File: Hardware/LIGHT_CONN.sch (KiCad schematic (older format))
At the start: 49 parts, among them P10 -15V, P11 ~4, P12 1, P13 ~5, P14 +5V, P18 RX7, P19 3.3V, P20 TX6, P21 1.8V, P22 PSU_CTL, P23 GND, P27 D1, P29 D2, P30 D3, P31 P1, P32 L1.8_1, P33 L3.3_1, P34 P2, P35 L1.8_2, P36 L3.3_2, P37 P3, P38 L1.8_3, P39 L3.3_3, P40 P4, P41 L1.8_4, P42 L3.3_4, P6 CONN_02X14, P7 ~2, P8 +15V, P9 ~3, U22 PCA9685BS

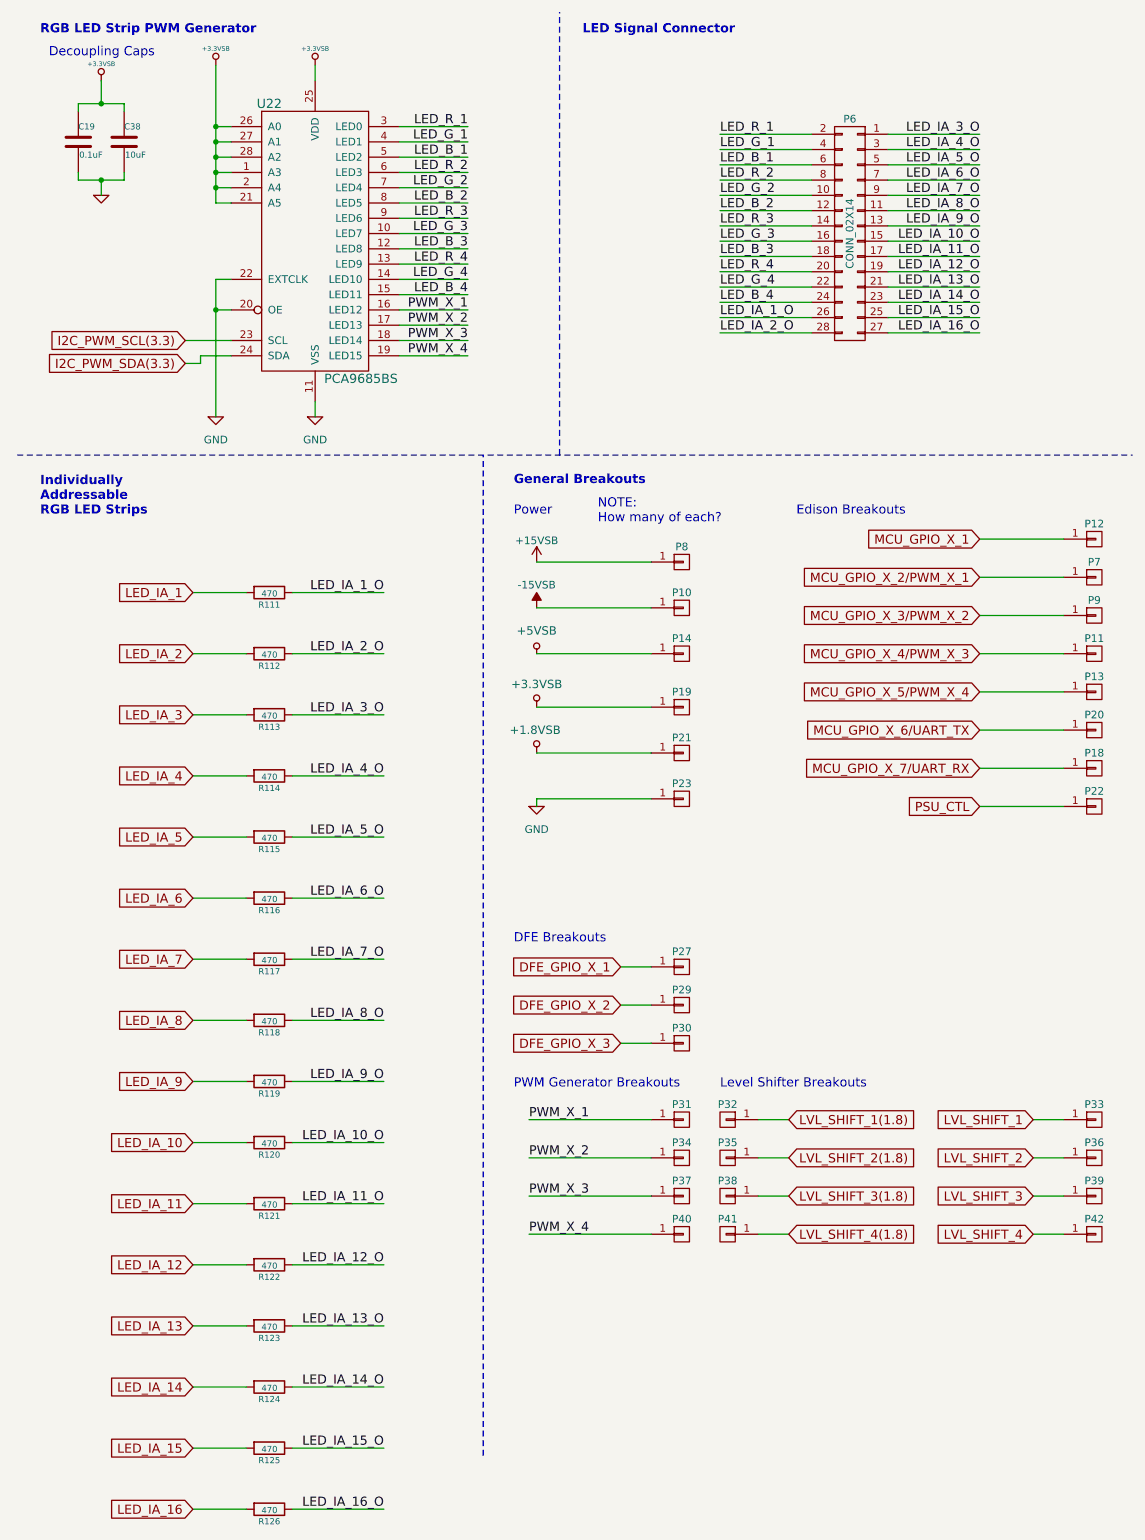
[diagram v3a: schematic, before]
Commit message: Digital Half completed placement
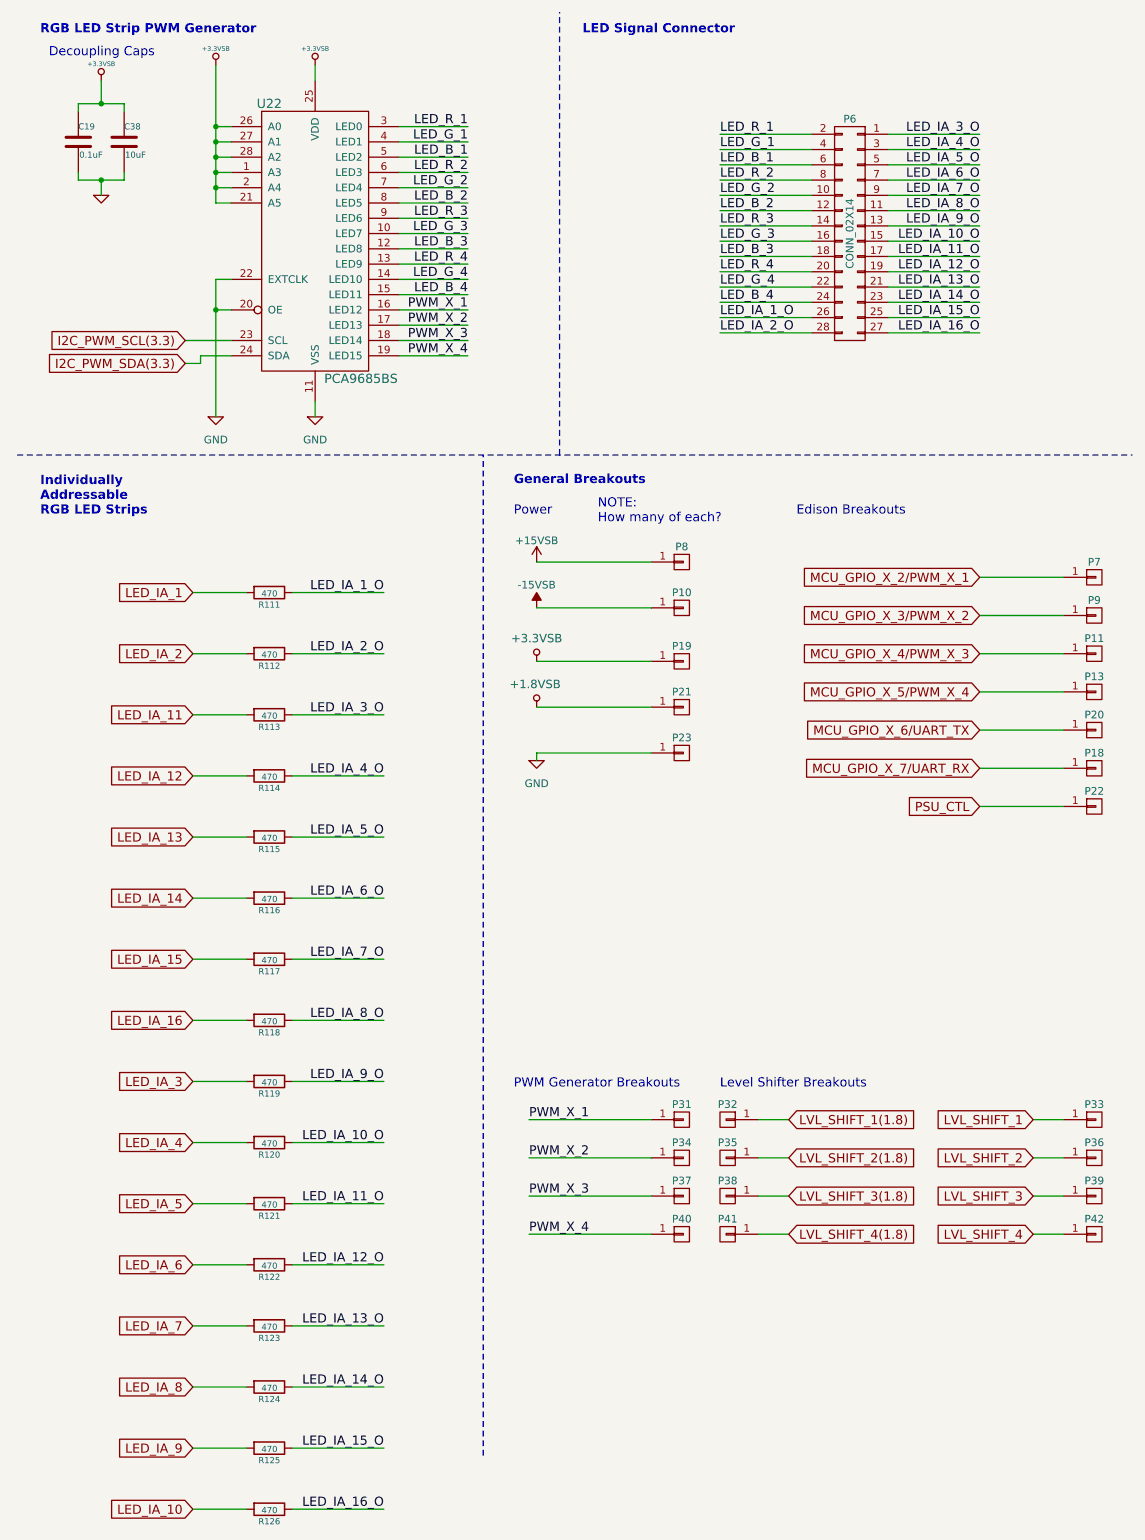
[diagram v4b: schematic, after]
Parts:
- removed P12: 1, Pin_Headers:Pin_Header_Straight_1x01, symbol CONN_01X01
- removed P14: +5V, Pin_Headers:Pin_Header_Straight_1x01, symbol CONN_01X01
- removed P27: D1, Pin_Headers:Pin_Header_Straight_1x01, symbol CONN_01X01
- removed P29: D2, Pin_Headers:Pin_Header_Straight_1x01, symbol CONN_01X01
- removed P30: D3, Pin_Headers:Pin_Header_Straight_1x01, symbol CONN_01X01
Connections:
- net LED_IA_10: now also R126.2; no longer R120.2
- net LED_IA_11: now also R113.2; no longer R121.2
- net LED_IA_12: now also R114.2; no longer R122.2
- net LED_IA_13: now also R115.2; no longer R123.2
- net LED_IA_14: now also R116.2; no longer R124.2
- net LED_IA_15: now also R117.2; no longer R125.2
- net LED_IA_16: now also R118.2; no longer R126.2
- net LED_IA_3: now also R119.2; no longer R113.2
- net LED_IA_4: now also R120.2; no longer R114.2
- net LED_IA_5: now also R121.2; no longer R115.2
- net LED_IA_6: now also R122.2; no longer R116.2
- net LED_IA_7: now also R123.2; no longer R117.2
- net LED_IA_8: now also R124.2; no longer R118.2
- net LED_IA_9: now also R125.2; no longer R119.2
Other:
- note removed: "DFE Breakouts"
- moved on the sheet: P19, P21, P23
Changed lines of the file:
@@
 $EndComp
 $Comp
-L GND-RESCUE-museV2-RESCUE-museV2 #PWR0118
+L GND-RESCUE-museV2-RESCUE-museV2 #PWR0114
 U 1 1 57E62373
 P 2450 3150
-F 0 "#PWR0118" H 2450 2900 50  0001 C CNN
+F 0 "#PWR0114" H 2450 2900 50  0001 C CNN
 F 1 "GND" H 2450 3000 50  0000 C CNN
 F 2 "" H 2450 3150 50  0000 C CNN
@@
 	1650 4700 2000 4700
 Wire Wire Line
+	1650 7500 2000 7500
+Wire Wire Line
+	1650 7900 2000 7900
+Wire Wire Line
+	1650 8300 2000 8300
+Wire Wire Line
+	1650 8700 2000 8700
+Wire Wire Line
+	1650 9100 2000 9100
+Wire Wire Line
+	1650 9500 2000 9500
+Wire Wire Line
+	1650 9900 2000 9900
+Wire Wire Line
+	1650 10300 2000 10300
+Wire Wire Line
 	1650 5100 2000 5100
 Wire Wire Line
@@
 Wire Wire Line
 	1650 7100 2000 7100
-Wire Wire Line
-	1650 7500 2000 7500
-Wire Wire Line
-	1650 7900 2000 7900
-Wire Wire Line
-	1650 8300 2000 8300
-Wire Wire Line
-	1650 8700 2000 8700
-Wire Wire Line
-	1650 9100 2000 9100
-Wire Wire Line
-	1650 9500 2000 9500
-Wire Wire Line
-	1650 9900 2000 9900
-Wire Wire Line
-	1650 10300 2000 10300
 Text Notes 650  650  0    60   ~ 12
 RGB LED Strip PWM Generator
@@
 Connection ~ 1800 1250
 $Comp
-L GND-RESCUE-museV2-RESCUE-museV2 #PWR0119
+L GND-RESCUE-museV2-RESCUE-museV2 #PWR0115
 U 1 1 57EF1660
 P 1800 3150
-F 0 "#PWR0119" H 1800 2900 50  0001 C CNN
+F 0 "#PWR0115" H 1800 2900 50  0001 C CNN
 F 1 "GND" H 1800 3000 50  0000 C CNN
 F 2 "" H 1800 3150 50  0000 C CNN
@@
 Text GLabel 1650 4700 0    60   Input ~ 0
 LED_IA_2
+Text GLabel 1650 7500 0    60   Input ~ 0
+LED_IA_3
+Text GLabel 1650 7900 0    60   Input ~ 0
+LED_IA_4
+Text GLabel 1650 8300 0    60   Input ~ 0
+LED_IA_5
+Text GLabel 1650 8700 0    60   Input ~ 0
+LED_IA_6
+Text GLabel 1650 9100 0    60   Input ~ 0
+LED_IA_7
+Text GLabel 1650 9500 0    60   Input ~ 0
+LED_IA_8
+Text GLabel 1650 9900 0    60   Input ~ 0
+LED_IA_9
+Text GLabel 1650 10300 0    60   Input ~ 0
+LED_IA_10
 Text GLabel 1650 5100 0    60   Input ~ 0
-LED_IA_3
+LED_IA_11
 Text GLabel 1650 5500 0    60   Input ~ 0
-LED_IA_4
+LED_IA_12
 Text GLabel 1650 5900 0    60   Input ~ 0
-LED_IA_5
+LED_IA_13
 Text GLabel 1650 6300 0    60   Input ~ 0
-LED_IA_6
+LED_IA_14
 Text GLabel 1650 6700 0    60   Input ~ 0
-LED_IA_7
+LED_IA_15
 Text GLabel 1650 7100 0    60   Input ~ 0
-LED_IA_8
-Text GLabel 1650 7500 0    60   Input ~ 0
-LED_IA_9
-Text GLabel 1650 7900 0    60   Input ~ 0
-LED_IA_10
-Text GLabel 1650 8300 0    60   Input ~ 0
-LED_IA_11
-Text GLabel 1650 8700 0    60   Input ~ 0
-LED_IA_12
-Text GLabel 1650 9100 0    60   Input ~ 0
-LED_IA_13
-Text GLabel 1650 9500 0    60   Input ~ 0
-LED_IA_14
-Text GLabel 1650 9900 0    60   Input ~ 0
-LED_IA_15
-Text GLabel 1650 10300 0    60   Input ~ 0
 LED_IA_16
 Wire Wire Line
@@
 $EndComp
 $Comp
-L +15VSB #PWR0120
+L +15VSB #PWR0116
 U 1 1 57FFBADE
 P 3900 4100
-F 0 "#PWR0120" H 3900 3950 50  0001 C CNN
+F 0 "#PWR0116" H 3900 3950 50  0001 C CNN
 F 1 "+15VSB" H 3900 4240 50  0000 C CNN
 F 2 "" H 3900 4100 50  0000 C CNN
@@
 	4650 4400 3900 4400
 $Comp
-L -15VSB #PWR134
+L -15VSB #PWR130
 U 1 1 57FFBC18
 P 3900 4400
-F 0 "#PWR134" H 3900 4500 50  0001 C CNN
+F 0 "#PWR130" H 3900 4500 50  0001 C CNN
 F 1 "-15VSB" H 3900 4550 50  0000 C CNN
 F 2 "" H 3900 4400 50  0000 C CNN
@@
 $EndComp
 $Comp
-L CONN_01X01 P14
-U 1 1 57FFBEAF
-P 4850 4700
-F 0 "P14" H 4850 4800 50  0000 C CNN
-F 1 "+5V" V 4950 4700 50  0001 C CNN
-F 2 "Pin_Headers:Pin_Header_Straight_1x01" H 4850 4700 50  0001 C CNN
-F 3 "" H 4850 4700 50  0000 C CNN
-	1    4850 4700
-	1    0    0    -1
-$EndComp
-Wire Wire Line
-	4650 4700 3900 4700
-$Comp
-L +5VSB #PWR0121
-U 1 1 57FFD044
-P 3900 4700
-F 0 "#PWR0121" H 3900 4790 20  0001 C CNN
-F 1 "+5VSB" H 3900 4850 55  0000 C CNN
-F 2 "" H 3900 4700 60  0000 C CNN
-F 3 "" H 3900 4700 60  0000 C CNN
-	1    3900 4700
-	1    0    0    -1
-$EndComp
-$Comp
 L CONN_01X01 P19
 U 1 1 57FFE1F7
+P 4850 4750
+F 0 "P19" H 4850 4850 50  0000 C CNN
+F 1 "3.3V" V 4950 4750 50  0001 C CNN
+F 2 "Pin_Headers:Pin_Header_Straight_1x01" H 4850 4750 50  0001 C CNN
+F 3 "" H 4850 4750 50  0000 C CNN
+	1    4850 4750
+	1    0    0    -1
+$EndComp
+Wire Wire Line
+	4650 4750 3900 4750
+$Comp
+L +3.3VSB #PWR0117
+U 1 1 57FFEA10
+P 3900 4750
+F 0 "#PWR0117" H 3900 4710 30  0001 C CNN
+F 1 "+3.3VSB" H 3900 4900 55  0000 C CNN
+F 2 "" H 3900 4750 60  0000 C CNN
+F 3 "" H 3900 4750 60  0000 C CNN
+	1    3900 4750
+	1    0    0    -1
+$EndComp
+$Comp
+L CONN_01X01 P21
+U 1 1 57FFEA97
 P 4850 5050
-F 0 "P19" H 4850 5150 50  0000 C CNN
-F 1 "3.3V" V 4950 5050 50  0001 C CNN
+F 0 "P21" H 4850 5150 50  0000 C CNN
+F 1 "1.8V" V 4950 5050 50  0001 C CNN
 F 2 "Pin_Headers:Pin_Header_Straight_1x01" H 4850 5050 50  0001 C CNN
 F 3 "" H 4850 5050 50  0000 C CNN
@@
 	4650 5050 3900 5050
 $Comp
-L +3.3VSB #PWR0122
-U 1 1 57FFEA10
+L +1.8VSB #PWR0118
+U 1 1 57FFEE42
 P 3900 5050
-F 0 "#PWR0122" H 3900 5010 30  0001 C CNN
-F 1 "+3.3VSB" H 3900 5200 55  0000 C CNN
+F 0 "#PWR0118" H 3900 5190 20  0001 C CNN
+F 1 "+1.8VSB" H 3890 5200 55  0000 C CNN
 F 2 "" H 3900 5050 60  0000 C CNN
 F 3 "" H 3900 5050 60  0000 C CNN
@@
 $EndComp
 $Comp
-L CONN_01X01 P21
-U 1 1 57FFEA97
+L CONN_01X01 P23
+U 1 1 57FFF0C1
 P 4850 5350
-F 0 "P21" H 4850 5450 50  0000 C CNN
-F 1 "1.8V" V 4950 5350 50  0001 C CNN
+F 0 "P23" H 4850 5450 50  0000 C CNN
+F 1 "GND" V 4950 5350 50  0001 C CNN
 F 2 "Pin_Headers:Pin_Header_Straight_1x01" H 4850 5350 50  0001 C CNN
 F 3 "" H 4850 5350 50  0000 C CNN
@@
 	4650 5350 3900 5350
 $Comp
-L +1.8VSB #PWR0123
-U 1 1 57FFEE42
-P 3900 5350
-F 0 "#PWR0123" H 3900 5490 20  0001 C CNN
-F 1 "+1.8VSB" H 3890 5500 55  0000 C CNN
-F 2 "" H 3900 5350 60  0000 C CNN
-F 3 "" H 3900 5350 60  0000 C CNN
-	1    3900 5350
-	1    0    0    -1
-$EndComp
-$Comp
-L CONN_01X01 P23
-U 1 1 57FFF0C1
-P 4850 5650
-F 0 "P23" H 4850 5750 50  0000 C CNN
-F 1 "GND" V 4950 5650 50  0001 C CNN
-F 2 "Pin_Headers:Pin_Header_Straight_1x01" H 4850 5650 50  0001 C CNN
-F 3 "" H 4850 5650 50  0000 C CNN
-	1    4850 5650
-	1    0    0    -1
-$EndComp
-Wire Wire Line
-	4650 5650 3900 5650
-$Comp
-L GND-RESCUE-museV2-RESCUE-museV2 #PWR0124
+L GND-RESCUE-museV2-RESCUE-museV2 #PWR0119
 U 1 1 57FFF105
-P 3900 5700
-F 0 "#PWR0124" H 3900 5450 50  0001 C CNN
-F 1 "GND" H 3900 5550 50  0000 C CNN
-F 2 "" H 3900 5700 50  0000 C CNN
-F 3 "" H 3900 5700 50  0000 C CNN
-	1    3900 5700
-	1    0    0    -1
-$EndComp
-Wire Wire Line
-	3900 5650 3900 5700
+P 3900 5400
+F 0 "#PWR0119" H 3900 5150 50  0001 C CNN
+F 1 "GND" H 3900 5250 50  0000 C CNN
+F 2 "" H 3900 5400 50  0000 C CNN
+F 3 "" H 3900 5400 50  0000 C CNN
+	1    3900 5400
+	1    0    0    -1
+$EndComp
+Wire Wire Line
+	3900 5350 3900 5400
 Text Notes 4300 3850 0    60   ~ 0
 NOTE:\nHow many of each?
 Text Notes 3750 3800 0    60   ~ 0
 Power
-Text GLabel 4450 6750 0    60   Input ~ 0
-DFE_GPIO_X_1
-Text GLabel 4450 7000 0    60   Input ~ 0
-DFE_GPIO_X_2
-Text GLabel 4450 7250 0    60   Input ~ 0
-DFE_GPIO_X_3
-$Comp
-L CONN_01X01 P30
-U 1 1 58004BCB
-P 4850 7250
-F 0 "P30" H 4850 7350 50  0000 C CNN
-F 1 "D3" V 4950 7250 50  0001 C CNN
-F 2 "Pin_Headers:Pin_Header_Straight_1x01" H 4850 7250 50  0001 C CNN
-F 3 "" H 4850 7250 50  0000 C CNN
-	1    4850 7250
-	1    0    0    -1
-$EndComp
-$Comp
-L CONN_01X01 P29
-U 1 1 58004C4E
-P 4850 7000
-F 0 "P29" H 4850 7100 50  0000 C CNN
-F 1 "D2" V 4950 7000 50  0001 C CNN
-F 2 "Pin_Headers:Pin_Header_Straight_1x01" H 4850 7000 50  0001 C CNN
-F 3 "" H 4850 7000 50  0000 C CNN
-	1    4850 7000
-	1    0    0    -1
-$EndComp
-$Comp
-L CONN_01X01 P27
-U 1 1 58004CB6
-P 4850 6750
-F 0 "P27" H 4850 6850 50  0000 C CNN
-F 1 "D1" V 4950 6750 50  0001 C CNN
-F 2 "Pin_Headers:Pin_Header_Straight_1x01" H 4850 6750 50  0001 C CNN
-F 3 "" H 4850 6750 50  0000 C CNN
-	1    4850 6750
-	1    0    0    -1
-$EndComp
-Wire Wire Line
-	4650 7000 4450 7000
-Wire Wire Line
-	4450 7250 4650 7250
-Text Notes 3750 6600 0    60   ~ 0
-DFE Breakouts
 Text Notes 5600 3800 0    60   ~ 0
 Edison Breakouts
@@
 Text GLabel 6800 5200 0    60   Input ~ 0
 MCU_GPIO_X_6/UART_TX
-Wire Wire Line
-	4450 6750 4650 6750
 Text Notes 5100 7550 0    60   ~ 0
 Level Shifter Breakouts
@@
 Text GLabel 6800 5700 0    60   Input ~ 0
 PSU_CTL
-Text GLabel 6800 3950 0    60   Input ~ 0
-MCU_GPIO_X_1
-$Comp
-L CONN_01X01 P12
-U 1 1 5862A3DE
-P 7550 3950
-F 0 "P12" H 7550 4050 50  0000 C CNN
-F 1 "1" V 7650 3950 50  0001 C CNN
-F 2 "Pin_Headers:Pin_Header_Straight_1x01" H 7550 3950 50  0001 C CNN
-F 3 "" H 7550 3950 50  0000 C CNN
-	1    7550 3950
-	1    0    0    -1
-$EndComp
-Wire Wire Line
-	7350 3950 6800 3950
-$Comp
-L +3.3VSB #PWR0125
+$Comp
+L +3.3VSB #PWR0120
 U 1 1 5862B130
 P 1800 850
-F 0 "#PWR0125" H 1800 810 30  0001 C CNN
+F 0 "#PWR0120" H 1800 810 30  0001 C CNN
 F 1 "+3.3VSB" H 1800 960 30  0000 C CNN
 F 2 "" H 1800 850 60  0000 C CNN
@@
 $EndComp
 $Comp
-L +3.3VSB #PWR0126
+L +3.3VSB #PWR0121
 U 1 1 5862B1CF
 P 2450 850
-F 0 "#PWR0126" H 2450 810 30  0001 C CNN
+F 0 "#PWR0121" H 2450 810 30  0001 C CNN
 F 1 "+3.3VSB" H 2450 960 30  0000 C CNN
 F 2 "" H 2450 850 60  0000 C CNN
@@
 $EndComp
 $Comp
-L +3.3VSB #PWR0127
+L +3.3VSB #PWR0122
 U 1 1 5862D3DB
 P 1050 950
-F 0 "#PWR0127" H 1050 910 30  0001 C CNN
+F 0 "#PWR0122" H 1050 910 30  0001 C CNN
 F 1 "+3.3VSB" H 1050 1060 30  0000 C CNN
 F 2 "" H 1050 950 60  0000 C CNN
@@
 	1200 1600 1200 1550
 $Comp
-L GND #PWR0128
+L GND #PWR0123
 U 1 1 5862D6A9
 P 1050 1700
-F 0 "#PWR0128" H 1050 1700 30  0001 C CNN
+F 0 "#PWR0123" H 1050 1700 30  0001 C CNN
 F 1 "GND" H 1050 1630 30  0001 C CNN
 F 2 "" H 1050 1700 60  0000 C CNN

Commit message: Beginning analog chip placement
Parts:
- C38: footprint Capacitors_SMD:C_1206 -> Capacitors_SMD:c_elec_4x5.3
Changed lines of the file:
@@
 F 0 "C38" H 1200 1450 40  0000 L CNN
 F 1 "10uF" H 1206 1265 40  0000 L CNN
-F 2 "Capacitors_SMD:C_1206" H 1238 1200 30  0001 C CNN
+F 2 "Capacitors_SMD:c_elec_4x5.3" H 1238 1200 30  0001 C CNN
 F 3 "" H 1200 1350 60  0000 C CNN
 	1    1200 1350

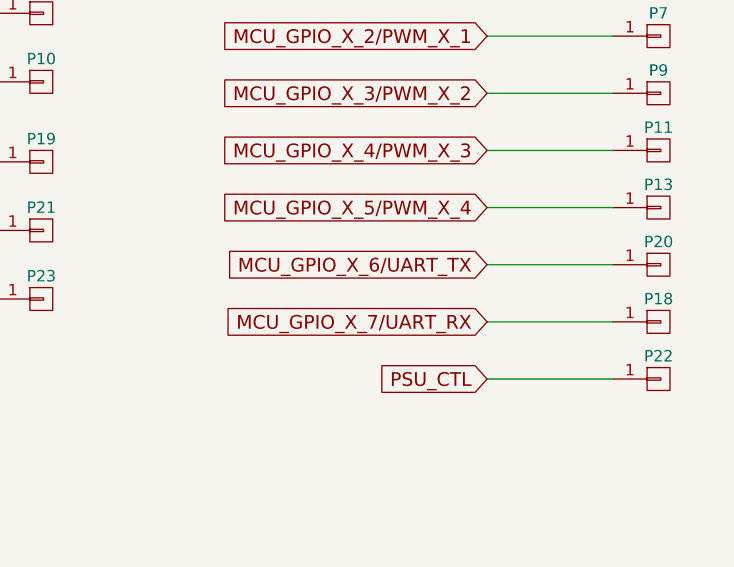
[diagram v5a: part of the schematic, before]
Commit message: All tracks and planes filled.  Fixing fill intersections and missing power/gnd connections
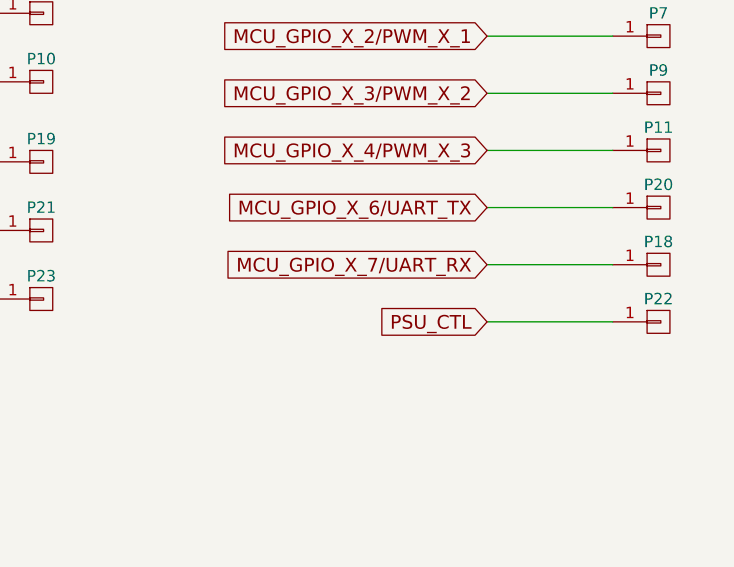
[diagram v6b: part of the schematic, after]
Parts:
- removed P13: ~5, Pin_Headers:Pin_Header_Straight_1x01, symbol CONN_01X01
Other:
- moved on the sheet: P18, P20, P22
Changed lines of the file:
@@
 Wire Wire Line
 	6800 4700 7350 4700
-$Comp
-L CONN_01X01 P13
-U 1 1 58007233
+Text GLabel 6800 5200 0    60   Input ~ 0
+MCU_GPIO_X_7/UART_RX
+$Comp
+L CONN_01X01 P20
+U 1 1 58007A71
 P 7550 4950
-F 0 "P13" H 7550 5050 50  0000 C CNN
-F 1 "~5" V 7650 4950 50  0001 C CNN
+F 0 "P20" H 7550 5050 50  0000 C CNN
+F 1 "TX6" V 7650 4950 50  0001 C CNN
 F 2 "Pin_Headers:Pin_Header_Straight_1x01" H 7550 4950 50  0001 C CNN
 F 3 "" H 7550 4950 50  0000 C CNN
@@
 	1    0    0    -1
 $EndComp
-Wire Wire Line
-	6800 4950 7350 4950
-Text GLabel 6800 4950 0    60   Input ~ 0
-MCU_GPIO_X_5/PWM_X_4
-Text GLabel 6800 5450 0    60   Input ~ 0
-MCU_GPIO_X_7/UART_RX
-$Comp
-L CONN_01X01 P20
-U 1 1 58007A71
+$Comp
+L CONN_01X01 P18
+U 1 1 58007A77
 P 7550 5200
-F 0 "P20" H 7550 5300 50  0000 C CNN
-F 1 "TX6" V 7650 5200 50  0001 C CNN
+F 0 "P18" H 7550 5300 50  0000 C CNN
+F 1 "RX7" V 7650 5200 50  0001 C CNN
 F 2 "Pin_Headers:Pin_Header_Straight_1x01" H 7550 5200 50  0001 C CNN
 F 3 "" H 7550 5200 50  0000 C CNN
@@
 	1    0    0    -1
 $EndComp
-$Comp
-L CONN_01X01 P18
-U 1 1 58007A77
-P 7550 5450
-F 0 "P18" H 7550 5550 50  0000 C CNN
-F 1 "RX7" V 7650 5450 50  0001 C CNN
-F 2 "Pin_Headers:Pin_Header_Straight_1x01" H 7550 5450 50  0001 C CNN
-F 3 "" H 7550 5450 50  0000 C CNN
-	1    7550 5450
-	1    0    0    -1
-$EndComp
-Wire Wire Line
-	6800 5450 7350 5450
-Wire Wire Line
-	7350 5200 6800 5200
-Text GLabel 6800 5200 0    60   Input ~ 0
+Wire Wire Line
+	6800 5200 7350 5200
+Wire Wire Line
+	7350 4950 6800 4950
+Text GLabel 6800 4950 0    60   Input ~ 0
 MCU_GPIO_X_6/UART_TX
 Text Notes 5100 7550 0    60   ~ 0
@@
 L CONN_01X01 P22
 U 1 1 585A0CF3
-P 7550 5700
-F 0 "P22" H 7550 5800 50  0000 C CNN
-F 1 "PSU_CTL" V 7650 5700 50  0001 C CNN
-F 2 "Pin_Headers:Pin_Header_Straight_1x01" H 7550 5700 50  0001 C CNN
-F 3 "" H 7550 5700 50  0000 C CNN
-	1    7550 5700
-	1    0    0    -1
-$EndComp
-Wire Wire Line
-	7350 5700 6800 5700
-Text GLabel 6800 5700 0    60   Input ~ 0
+P 7550 5450
+F 0 "P22" H 7550 5550 50  0000 C CNN
+F 1 "PSU_CTL" V 7650 5450 50  0001 C CNN
+F 2 "Pin_Headers:Pin_Header_Straight_1x01" H 7550 5450 50  0001 C CNN
+F 3 "" H 7550 5450 50  0000 C CNN
+	1    7550 5450
+	1    0    0    -1
+$EndComp
+Wire Wire Line
+	7350 5450 6800 5450
+Text GLabel 6800 5450 0    60   Input ~ 0
 PSU_CTL
 $Comp
